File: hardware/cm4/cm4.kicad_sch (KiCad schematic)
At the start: 14 parts, among them J11 CM4 Stecker 1, J12 CM4 Stecker 2, Q10 BSS84

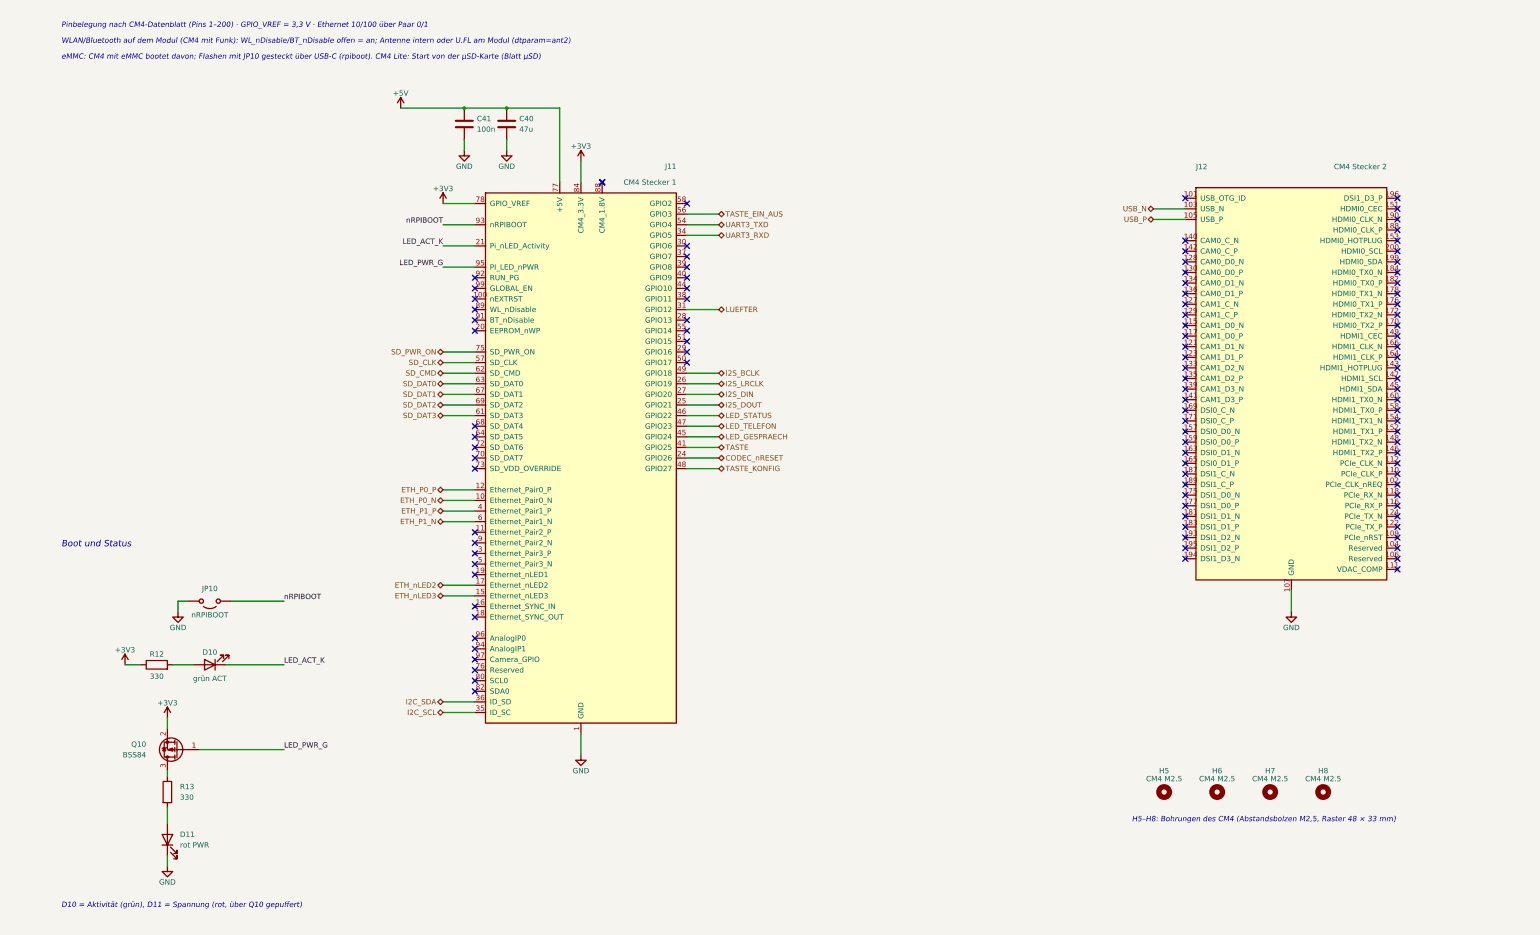
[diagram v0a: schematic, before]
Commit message: CM4-Träger: 4P4C statt DE9, CM4-Platzhalter, ausgerichtete 3D-Modelle
- Serielle Buchse J3: Würth 615004143821 (4P4C), Adapterkabel auf DE9; HAT behält DE9
- M1: CM4 als Platzhalter (Stückliste ja, Bestückungsdaten nein), offizielles STEP 1,5 mm über J11/J12
- 3D-Modelle (Würth RJ45/RJ12/RJ10, Hirose DF40, Bourns SM-LP-5001, ECS-Oszillator) als
  Modellparameter, jede Lage im Rendering geprüft; Herstellermodelle nur lokal (QUELLEN.md)
- richte_3d_aus.py: CM4-Modell laden/verschieben, Lagedatei für die Footprints
- Neu geroutet (0,127 mm Standard), DRC ohne Verstöße, 0 offene Verbindungen

Co-Authored-By: Claude Opus 5.5 <noreply@anthropic.com>
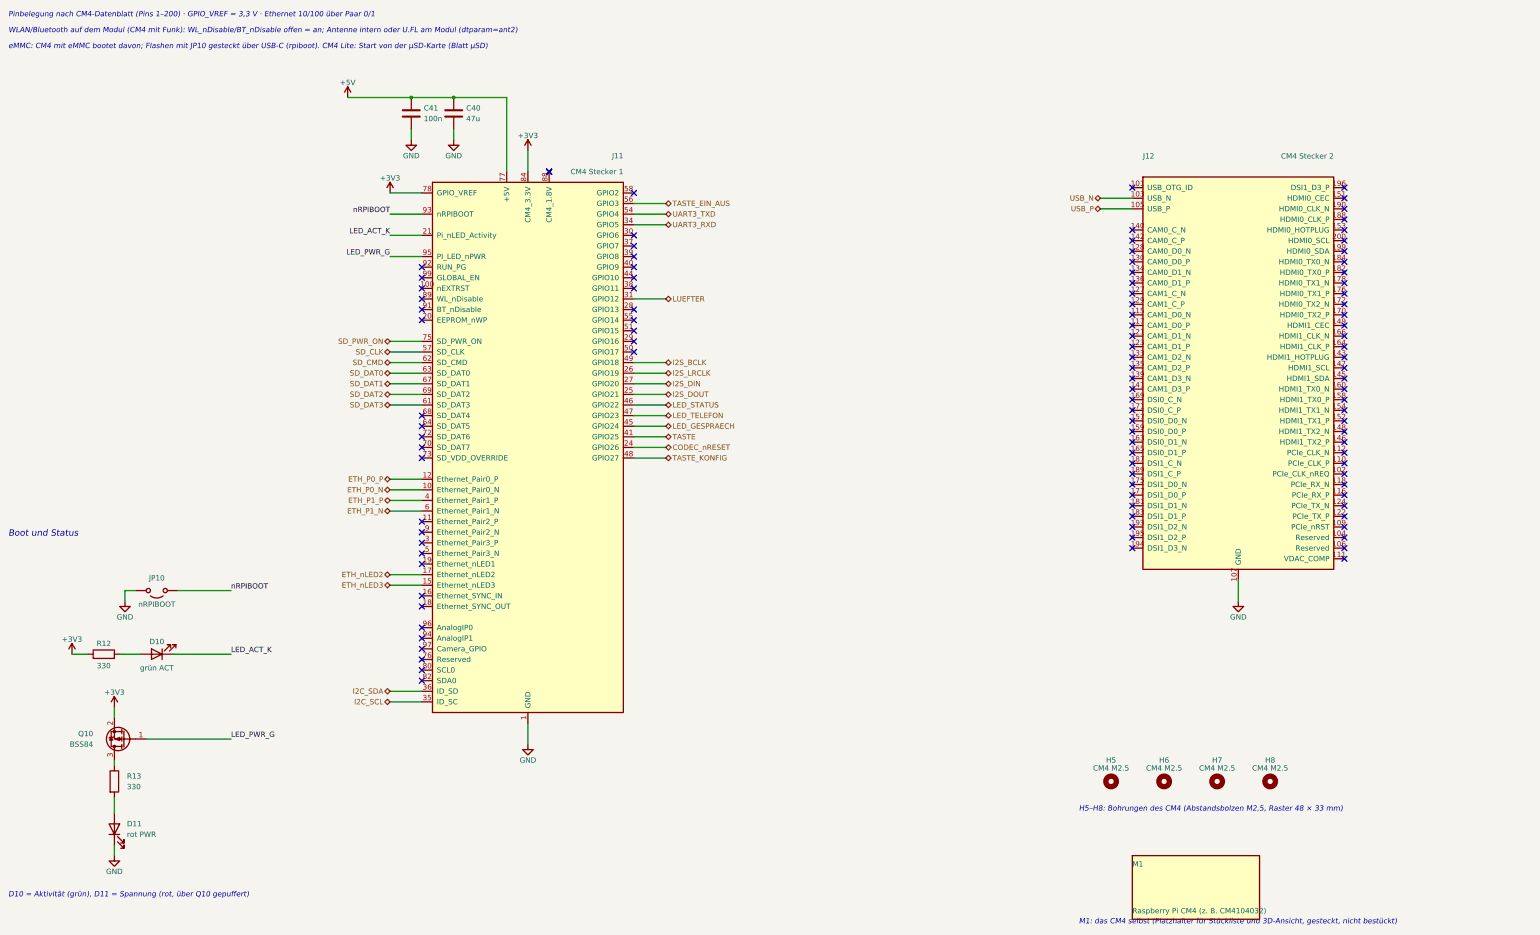
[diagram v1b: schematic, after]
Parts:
- added M1: Raspberry Pi CM4 (z. B. CM4104032), Sopho2SIP:CM4_Modul_Platzhalter, symbol Sopho2SIP:CM4_Modul
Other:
- note added: "M1: das CM4 selbst (Platzhalter für Stückliste und 3D-Ansicht, gesteckt, nicht bestückt)"
- moved on the sheet: C40, C41, D10, D11, H5, H6, H7, H8, J11, J12, JP10, Q10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
